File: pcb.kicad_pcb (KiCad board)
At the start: 2 copper layers, 139.8 x 95.8 mm, 43 parts

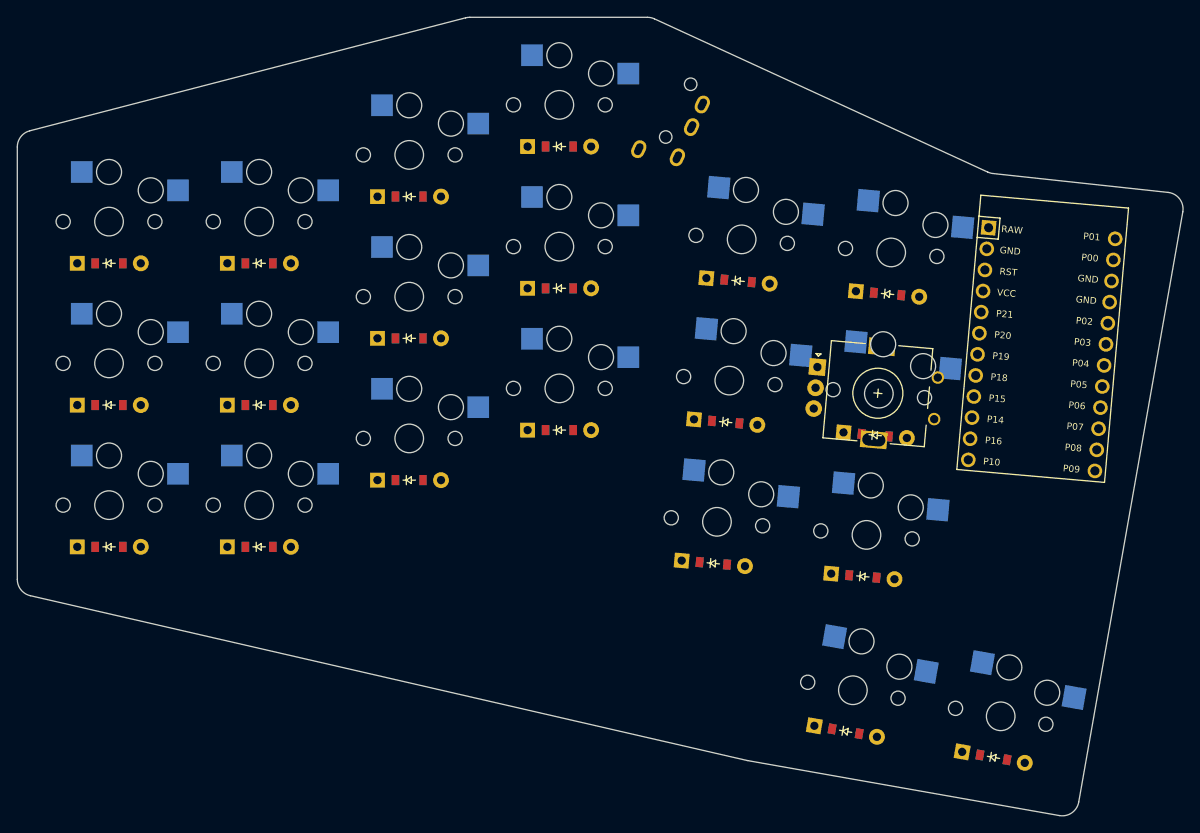
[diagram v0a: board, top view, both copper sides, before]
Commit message: begun creation of schematic, probably willl have to overhaul pcb
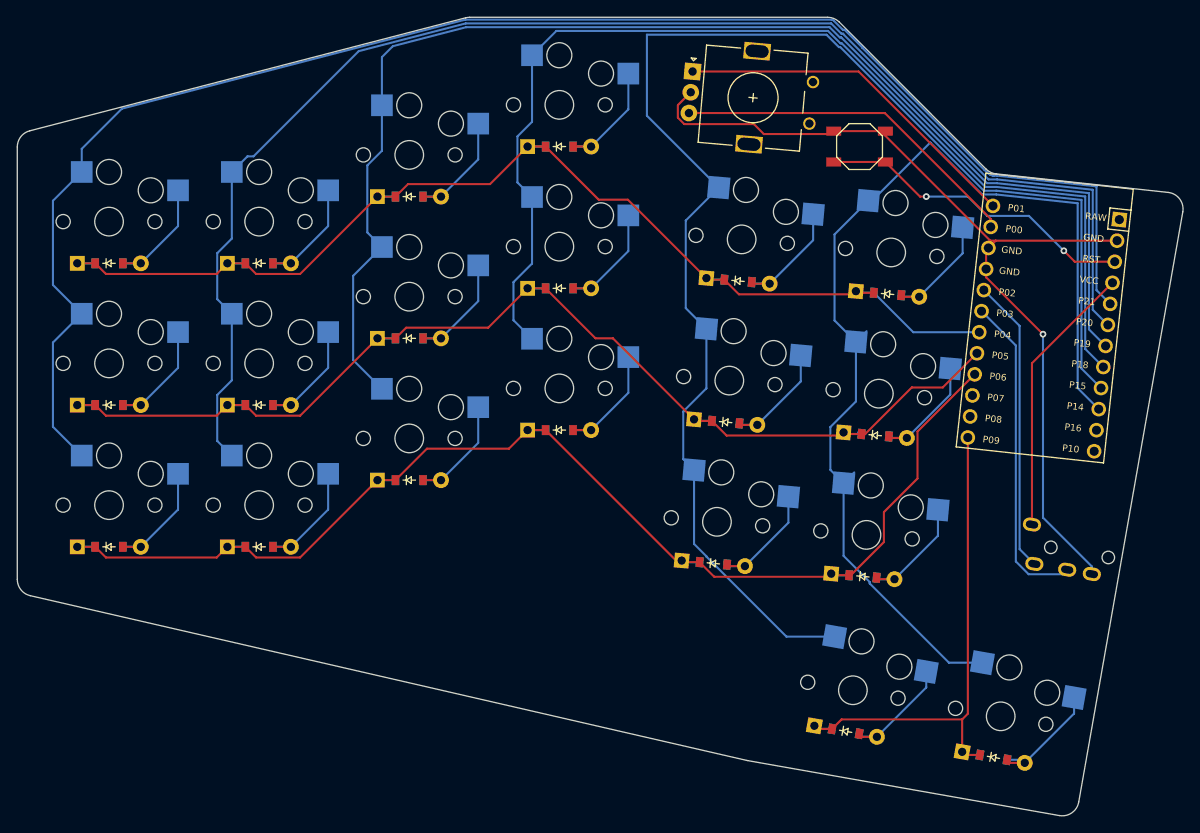
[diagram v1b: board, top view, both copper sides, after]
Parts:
- added B1: , E73:SW_TACT_ALPS_SKQGABE010, F.Cu at (190.0, 57.0)
- moved TRRS1 77.0 mm to (221.0, 108.8), turned to -100 degrees
- moved ROT1 38.5 mm to (177.3, 51.2)
- moved MCU1 2.50 mm to (212.1, 78.8), turned to -96.2 degrees
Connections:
- D1 pad 1: (no net) -> P6
- D10 pad 1: (no net) -> P6
- D11 pad 1: (no net) -> P5
- D12 pad 1: (no net) -> P4
- D13 pad 1: (no net) -> P6
- D14 pad 1: (no net) -> P5
- D15 pad 1: (no net) -> P4
- D16 pad 1: (no net) -> P6
- D17 pad 1: (no net) -> P5
- D18 pad 1: (no net) -> P4
- D19 pad 1: (no net) -> P9
- D2 pad 1: (no net) -> P5
- D20 pad 1: (no net) -> P9
- D3 pad 1: (no net) -> P4
- D4 pad 1: (no net) -> P6
- D5 pad 1: (no net) -> P5
- D6 pad 1: (no net) -> P4
- D7 pad 1: (no net) -> P6
- D8 pad 1: (no net) -> P5
- D9 pad 1: (no net) -> P4
- ROT1 pad 1: p5 -> empty
- ROT1 pad 2: p5 -> empty i think
- ROT1 pad A: s -> P1
- ROT1 pad B: d -> P0
- ROT1 pad C: g -> GND
- S1 pad 1: (no net) -> P21
- S10 pad 1: (no net) -> P18
- S11 pad 1: (no net) -> P18
- S12 pad 1: (no net) -> P18
- S13 pad 1: (no net) -> P15
- S14 pad 1: (no net) -> P15
- S15 pad 1: (no net) -> P15
- S16 pad 1: (no net) -> P14
- S17 pad 1: (no net) -> P14
- S18 pad 1: (no net) -> P14
- S19 pad 1: (no net) -> P15
- S2 pad 1: (no net) -> P21
- S20 pad 1: (no net) -> P14
- S3 pad 1: (no net) -> P21
- S4 pad 1: (no net) -> P20
- S5 pad 1: (no net) -> P20
- S6 pad 1: (no net) -> P20
- S7 pad 1: (no net) -> P19
- S8 pad 1: (no net) -> P19
- S9 pad 1: (no net) -> P19
- TRRS1 pad 1: idk -> VCC
- TRRS1 pad 2: idek -> P2
- TRRS1 pad 3: IEek -> P3
- TRRS1 pad 4: idee -> GND
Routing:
- net P21: track 0.00 -> 190.1 mm
- net P15: track 0.00 -> 173.9 mm
- net P20: track 0.00 -> 171.4 mm
- net P19: track 0.00 -> 156.7 mm
- net P6: track 0.00 -> 151.5 mm
- net P5: track 0.00 -> 141.0 mm
- net P4: track 0.00 -> 138.7 mm
- net P18: track 0.00 -> 134.0 mm
- net P14: track 0.00 -> 129.6 mm
- net GND: track 0.00 -> 108.8 mm, vias 0 -> 1
- net P9: track 0.00 -> 63.2 mm
- net P1: track 0.00 -> 42.7 mm
- net P0: track 0.00 -> 42.4 mm
- net P3: track 0.00 -> 38.7 mm
- net RST: track 0.00 -> 38.7 mm, vias 0 -> 2
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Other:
- outline, holes or cut-outs redrawn
- net class Default removed
